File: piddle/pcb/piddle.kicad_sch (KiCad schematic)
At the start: 58 parts, among them J1 Conn_01x03_Socket, J10 Conn_01x03_Socket, J11 Conn_01x03_Socket, J12 Conn_01x03_Socket, J13 Conn_01x03_Socket, J14 Conn_01x03_Socket, J15 Conn_01x03_Socket, J16 infrared receiver, J17 5v, J18 3v3, J19 5v, J2 Conn_01x03_Socket, J20 JST power 1, J21 JST power 2, J22 5V in jumper from LED strip, J23 GPIOs, J24 radio receiver, J25 JST power 3, J3 Conn_01x03_Socket, J4 Conn_01x03_Socket, J5 Conn_01x03_Socket, J6 Conn_01x03_Socket, J7 Conn_01x03_Socket, J8 Conn_01x03_Socket, J9 Conn_01x03_Socket, U1 ESP32-DevKitC, U2 INMP441

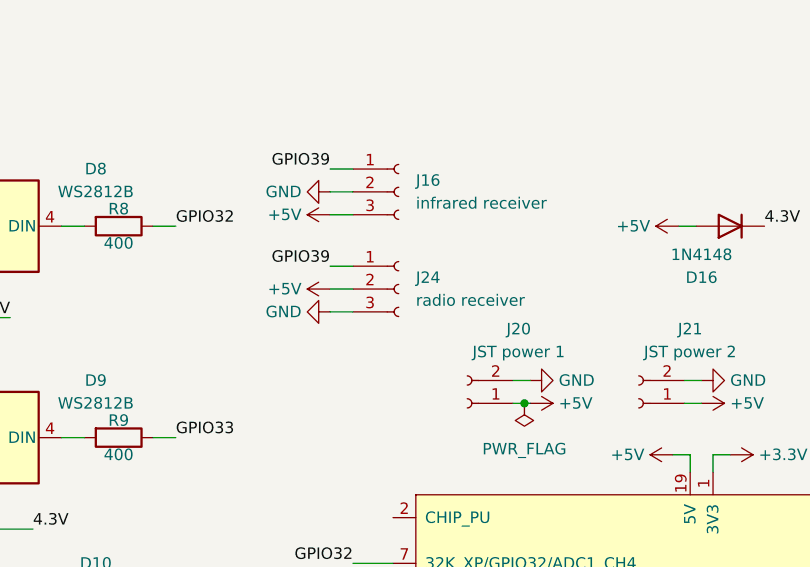
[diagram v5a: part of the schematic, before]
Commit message: Move pins around for RF radio module
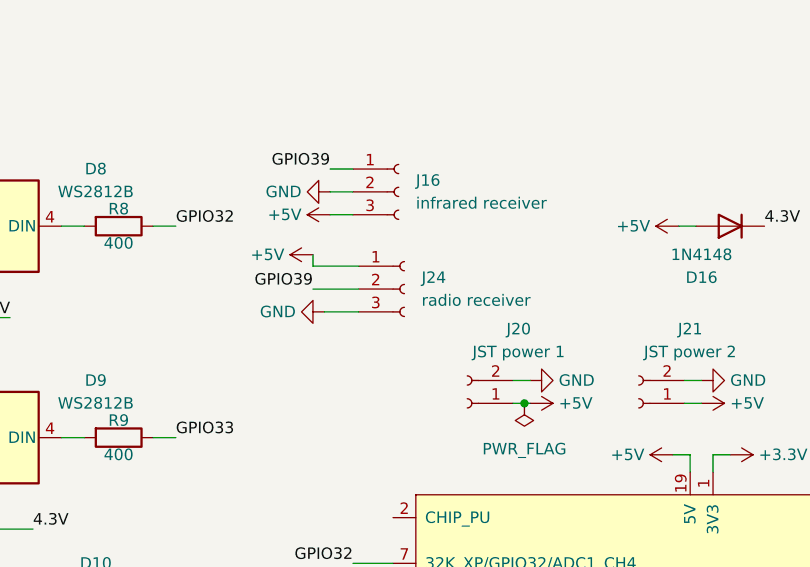
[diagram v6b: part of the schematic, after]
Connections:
- net +5V: now also J24.1 (Pin_1); no longer J24.2 (Pin_2)
- net GPIO39: now also J24.2 (Pin_2); no longer J24.1 (Pin_1)
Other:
- moved on the sheet: J24
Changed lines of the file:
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@@
 	(wire
 		(pts
-			(xy 172.72 115.57) (xy 176.53 115.57)
+			(xy 102.87 26.67) (xy 97.79 26.67)
 		)
 		(stroke
@@
 	(wire
 		(pts
-			(xy 158.75 41.91) (xy 160.655 41.91)
+			(xy 172.72 115.57) (xy 176.53 115.57)
 		)
 		(stroke
@@
 	(wire
 		(pts
-			(xy 99.695 26.67) (xy 102.235 26.67)
+			(xy 158.75 41.91) (xy 160.655 41.91)
 		)
 		(stroke
@@
 	(wire
 		(pts
+			(xy 97.79 26.67) (xy 97.79 25.4)
+		)
+		(stroke
+			(width 0)
+			(type default)
+		)
+	)
+	(wire
+		(pts
 			(xy 223.52 17.78) (xy 224.79 17.78)
 		)
@@
 	(wire
 		(pts
+			(xy 99.06 31.75) (xy 102.87 31.75)
+		)
+		(stroke
+			(width 0)
+			(type default)
+		)
+	)
+	(wire
+		(pts
 			(xy 213.36 55.88) (xy 215.9 55.88)
 		)
@@
 	(wire
 		(pts
-			(xy 137.795 47.625) (xy 139.7 47.625)
+			(xy 97.79 29.21) (xy 102.87 29.21)
 		)
 		(stroke
@@
 	(wire
 		(pts
-			(xy 235.585 103.505) (xy 231.14 103.505)
+			(xy 137.795 47.625) (xy 139.7 47.625)
 		)
 		(stroke
@@
 	(wire
 		(pts
-			(xy 50.165 155.575) (xy 50.165 156.845)
+			(xy 235.585 103.505) (xy 231.14 103.505)
 		)
 		(stroke
@@
 	(wire
 		(pts
-			(xy 223.52 45.72) (xy 223.52 48.26)
+			(xy 50.165 155.575) (xy 50.165 156.845)
 		)
 		(stroke
@@
 	(wire
 		(pts
-			(xy 105.41 169.545) (xy 107.95 169.545)
+			(xy 223.52 45.72) (xy 223.52 48.26)
 		)
 		(stroke
@@
 	(wire
 		(pts
-			(xy 223.52 93.345) (xy 223.52 95.885)
+			(xy 105.41 169.545) (xy 107.95 169.545)
 		)
 		(stroke
@@
 	(wire
 		(pts
-			(xy 72.39 66.04) (xy 69.85 66.04)
+			(xy 223.52 93.345) (xy 223.52 95.885)
 		)
 		(stroke
@@
 	(wire
 		(pts
-			(xy 121.285 41.91) (xy 121.92 41.91)
+			(xy 72.39 66.04) (xy 69.85 66.04)
 		)
 		(stroke
@@
 	(wire
 		(pts
-			(xy 99.695 29.21) (xy 102.235 29.21)
+			(xy 121.285 41.91) (xy 121.92 41.91)
 		)
 		(stroke
@@
 	(wire
 		(pts
-			(xy 99.695 31.75) (xy 102.235 31.75)
-		)
-		(stroke
-			(width 0)
-			(type default)
-		)
-	)
-	(wire
-		(pts
 			(xy 221.615 93.345) (xy 223.52 93.345)
 		)
@@
 	)
 	(label "GPIO39"
-		(at 99.695 26.67 180)
+		(at 97.79 29.21 180)
 		(effects
 			(font
@@
 	(symbol
 		(lib_id "power:+5V")
-		(at 99.695 29.21 90)
+		(at 97.79 25.4 90)
 		(unit 1)
 		(exclude_from_sim no)
@@
 		(on_board yes)
 		(dnp no)
-		(fields_autoplaced yes)
 		(property "Reference" "#PWR032"
-			(at 103.505 29.21 0)
+			(at 101.6 25.4 0)
 			(effects
 				(font
@@
 		)
 		(property "Value" "+5V"
-			(at 96.52 29.21 90)
+			(at 94.615 25.4 90)
 			(effects
 				(font
@@
 		)
 		(property "Footprint" ""
-			(at 99.695 29.21 0)
+			(at 97.79 25.4 0)
 			(effects
 				(font
@@
 		)
 		(property "Datasheet" ""
-			(at 99.695 29.21 0)
+			(at 97.79 25.4 0)
 			(effects
 				(font
@@
 		)
 		(property "Description" ""
-			(at 99.695 29.21 0)
+			(at 97.79 25.4 0)
 			(effects
 				(font
@@
 	(symbol
 		(lib_id "Connector:Conn_01x03_Socket")
-		(at 107.315 29.21 0)
+		(at 107.95 29.21 0)
 		(unit 1)
 		(exclude_from_sim no)
@@
 		(fields_autoplaced yes)
 		(property "Reference" "J24"
-			(at 109.22 27.94 0)
+			(at 109.855 27.94 0)
 			(effects
 				(font
@@
 		)
 		(property "Value" "radio receiver"
-			(at 109.22 30.48 0)
+			(at 109.855 30.48 0)
 			(effects
 				(font
@@
 		)
 		(property "Footprint" "Connector_PinHeader_2.54mm:PinHeader_1x03_P2.54mm_Vertical"
-			(at 107.315 29.21 0)
+			(at 107.95 29.21 0)
 			(effects
 				(font
@@
 		)
 		(property "Datasheet" "~"
-			(at 107.315 29.21 0)
+			(at 107.95 29.21 0)
 			(effects
 				(font
@@
 		)
 		(property "Description" ""
-			(at 107.315 29.21 0)
+			(at 107.95 29.21 0)
 			(effects
 				(font
@@
 	(symbol
 		(lib_id "power:GND")
-		(at 99.695 31.75 270)
+		(at 99.06 31.75 270)
 		(unit 1)
 		(exclude_from_sim no)
@@
 		(dnp no)
 		(property "Reference" "#PWR031"
-			(at 93.345 31.75 0)
+			(at 92.71 31.75 0)
 			(effects
 				(font
@@
 		)
 		(property "Value" "GND"
-			(at 96.52 31.75 90)
+			(at 95.885 31.75 90)
 			(effects
 				(font
@@
 		)
 		(property "Footprint" ""
-			(at 99.695 31.75 0)
+			(at 99.06 31.75 0)
 			(effects
 				(font
@@
 		)
 		(property "Datasheet" ""
-			(at 99.695 31.75 0)
+			(at 99.06 31.75 0)
 			(effects
 				(font
@@
 		)
 		(property "Description" ""
-			(at 99.695 31.75 0)
+			(at 99.06 31.75 0)
 			(effects
 				(font

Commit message: Don't use pins used by WiFi
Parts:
- D1, D10, D11, D12, D13, D14, D15, D2, D3, D4, D5, D6, D7, D8, D9: footprint LED_SMD:LED_WS2812B_PLCC4_5.0x5.0mm_P3.2mm -> PCM_JLCPCB:LED_WS2812B_PLCC4_5.0x5.0mm_P3.2mm
- R1, R10, R11, R12, R13, R14, R15, R2, R3, R4, R5, R6, R7, R8, R9: footprint Resistor_THT:R_Axial_DIN0207_L6.3mm_D2.5mm_P10.16mm_Horizontal -> PCM_JLCPCB:R_1206
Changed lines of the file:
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@@
 			)
 		)
-		(property "Footprint" "LED_SMD:LED_WS2812B_PLCC4_5.0x5.0mm_P3.2mm"
+		(property "Footprint" "PCM_JLCPCB:LED_WS2812B_PLCC4_5.0x5.0mm_P3.2mm"
 			(at 224.79 159.385 0)
 			(effects
@@
 			)
 		)
-		(property "Footprint" "Resistor_THT:R_Axial_DIN0207_L6.3mm_D2.5mm_P10.16mm_Horizontal"
+		(property "Footprint" "PCM_JLCPCB:R_1206"
 			(at 209.55 130.683 90)
 			(effects
@@
 			)
 		)
-		(property "Footprint" "Resistor_THT:R_Axial_DIN0207_L6.3mm_D2.5mm_P10.16mm_Horizontal"
+		(property "Footprint" "PCM_JLCPCB:R_1206"
 			(at 209.55 77.597 90)
 			(effects
@@
 			)
 		)
-		(property "Footprint" "Resistor_THT:R_Axial_DIN0207_L6.3mm_D2.5mm_P10.16mm_Horizontal"
+		(property "Footprint" "PCM_JLCPCB:R_1206"
 			(at 76.2 64.262 90)
 			(effects
@@
 			)
 		)
-		(property "Footprint" "Resistor_THT:R_Axial_DIN0207_L6.3mm_D2.5mm_P10.16mm_Horizontal"
+		(property "Footprint" "PCM_JLCPCB:R_1206"
 			(at 209.55 57.658 90)
 			(effects
@@
 			)
 		)
-		(property "Footprint" "Resistor_THT:R_Axial_DIN0207_L6.3mm_D2.5mm_P10.16mm_Horizontal"
+		(property "Footprint" "PCM_JLCPCB:R_1206"
 			(at 76.2 182.372 90)
 			(effects
@@
 			)
 		)
-		(property "Footprint" "Resistor_THT:R_Axial_DIN0207_L6.3mm_D2.5mm_P10.16mm_Horizontal"
+		(property "Footprint" "PCM_JLCPCB:R_1206"
 			(at 76.2 129.667 90)
 			(effects
@@
 			)
 		)
-		(property "Footprint" "LED_SMD:LED_WS2812B_PLCC4_5.0x5.0mm_P3.2mm"
+		(property "Footprint" "PCM_JLCPCB:LED_WS2812B_PLCC4_5.0x5.0mm_P3.2mm"
 			(at 60.96 123.825 0)
 			(effects
@@
 			)
 		)
-		(property "Footprint" "LED_SMD:LED_WS2812B_PLCC4_5.0x5.0mm_P3.2mm"
+		(property "Footprint" "PCM_JLCPCB:LED_WS2812B_PLCC4_5.0x5.0mm_P3.2mm"
 			(at 224.79 136.525 0)
 			(effects
@@
 			)
 		)
-		(property "Footprint" "LED_SMD:LED_WS2812B_PLCC4_5.0x5.0mm_P3.2mm"
+		(property "Footprint" "PCM_JLCPCB:LED_WS2812B_PLCC4_5.0x5.0mm_P3.2mm"
 			(at 60.96 101.6 0)
 			(effects
@@
 			)
 		)
-		(property "Footprint" "LED_SMD:LED_WS2812B_PLCC4_5.0x5.0mm_P3.2mm"
+		(property "Footprint" "PCM_JLCPCB:LED_WS2812B_PLCC4_5.0x5.0mm_P3.2mm"
 			(at 224.79 111.125 0)
 			(effects
@@
 			)
 		)
-		(property "Footprint" "Resistor_THT:R_Axial_DIN0207_L6.3mm_D2.5mm_P10.16mm_Horizontal"
+		(property "Footprint" "PCM_JLCPCB:R_1206"
 			(at 209.55 11.938 90)
 			(effects
@@
 			)
 		)
-		(property "Footprint" "Resistor_THT:R_Axial_DIN0207_L6.3mm_D2.5mm_P10.16mm_Horizontal"
+		(property "Footprint" "PCM_JLCPCB:R_1206"
 			(at 209.55 35.433 90)
 			(effects
@@
 			)
 		)
-		(property "Footprint" "LED_SMD:LED_WS2812B_PLCC4_5.0x5.0mm_P3.2mm"
+		(property "Footprint" "PCM_JLCPCB:LED_WS2812B_PLCC4_5.0x5.0mm_P3.2mm"
 			(at 60.96 38.1 0)
 			(effects
@@
 			)
 		)
-		(property "Footprint" "Resistor_THT:R_Axial_DIN0207_L6.3mm_D2.5mm_P10.16mm_Horizontal"
+		(property "Footprint" "PCM_JLCPCB:R_1206"
 			(at 209.55 153.543 90)
 			(effects
@@
 			)
 		)
-		(property "Footprint" "Resistor_THT:R_Axial_DIN0207_L6.3mm_D2.5mm_P10.16mm_Horizontal"
+		(property "Footprint" "PCM_JLCPCB:R_1206"
 			(at 209.55 105.283 90)
 			(effects
@@
 			)
 		)
-		(property "Footprint" "LED_SMD:LED_WS2812B_PLCC4_5.0x5.0mm_P3.2mm"
+		(property "Footprint" "PCM_JLCPCB:LED_WS2812B_PLCC4_5.0x5.0mm_P3.2mm"
 			(at 60.96 80.01 0)
 			(effects
@@
 			)
 		)
-		(property "Footprint" "LED_SMD:LED_WS2812B_PLCC4_5.0x5.0mm_P3.2mm"
+		(property "Footprint" "PCM_JLCPCB:LED_WS2812B_PLCC4_5.0x5.0mm_P3.2mm"
 			(at 224.79 86.995 0)
 			(effects
@@
 			)
 		)
-		(property "Footprint" "LED_SMD:LED_WS2812B_PLCC4_5.0x5.0mm_P3.2mm"
+		(property "Footprint" "PCM_JLCPCB:LED_WS2812B_PLCC4_5.0x5.0mm_P3.2mm"
 			(at 60.96 58.42 0)
 			(effects
@@
 			)
 		)
-		(property "Footprint" "LED_SMD:LED_WS2812B_PLCC4_5.0x5.0mm_P3.2mm"
+		(property "Footprint" "PCM_JLCPCB:LED_WS2812B_PLCC4_5.0x5.0mm_P3.2mm"
 			(at 60.96 14.605 0)
 			(effects
@@
 			)
 		)
-		(property "Footprint" "Resistor_THT:R_Axial_DIN0207_L6.3mm_D2.5mm_P10.16mm_Horizontal"
+		(property "Footprint" "PCM_JLCPCB:R_1206"
 			(at 76.2 43.942 90)
 			(effects
@@
 			)
 		)
-		(property "Footprint" "Resistor_THT:R_Axial_DIN0207_L6.3mm_D2.5mm_P10.16mm_Horizontal"
+		(property "Footprint" "PCM_JLCPCB:R_1206"
 			(at 76.2 85.852 90)
 			(effects
@@
 			)
 		)
-		(property "Footprint" "LED_SMD:LED_WS2812B_PLCC4_5.0x5.0mm_P3.2mm"
+		(property "Footprint" "PCM_JLCPCB:LED_WS2812B_PLCC4_5.0x5.0mm_P3.2mm"
 			(at 60.96 176.53 0)
 			(effects
@@
 			)
 		)
-		(property "Footprint" "LED_SMD:LED_WS2812B_PLCC4_5.0x5.0mm_P3.2mm"
+		(property "Footprint" "PCM_JLCPCB:LED_WS2812B_PLCC4_5.0x5.0mm_P3.2mm"
 			(at 224.79 17.78 0)
 			(effects
@@
 			)
 		)
-		(property "Footprint" "LED_SMD:LED_WS2812B_PLCC4_5.0x5.0mm_P3.2mm"
+		(property "Footprint" "PCM_JLCPCB:LED_WS2812B_PLCC4_5.0x5.0mm_P3.2mm"
 			(at 224.79 63.5 0)
 			(effects
@@
 			)
 		)
-		(property "Footprint" "LED_SMD:LED_WS2812B_PLCC4_5.0x5.0mm_P3.2mm"
+		(property "Footprint" "PCM_JLCPCB:LED_WS2812B_PLCC4_5.0x5.0mm_P3.2mm"
 			(at 60.96 145.415 0)
 			(effects
@@
 			)
 		)
-		(property "Footprint" "Resistor_THT:R_Axial_DIN0207_L6.3mm_D2.5mm_P10.16mm_Horizontal"
+		(property "Footprint" "PCM_JLCPCB:R_1206"
 			(at 76.2 20.447 90)
 			(effects
@@
 			)
 		)
-		(property "Footprint" "LED_SMD:LED_WS2812B_PLCC4_5.0x5.0mm_P3.2mm"
+		(property "Footprint" "PCM_JLCPCB:LED_WS2812B_PLCC4_5.0x5.0mm_P3.2mm"
 			(at 224.79 41.275 0)
 			(effects
@@
 			)
 		)
-		(property "Footprint" "Resistor_THT:R_Axial_DIN0207_L6.3mm_D2.5mm_P10.16mm_Horizontal"
+		(property "Footprint" "PCM_JLCPCB:R_1206"
 			(at 76.2 107.442 90)
 			(effects
@@
 			)
 		)
-		(property "Footprint" "Resistor_THT:R_Axial_DIN0207_L6.3mm_D2.5mm_P10.16mm_Horizontal"
+		(property "Footprint" "PCM_JLCPCB:R_1206"
 			(at 76.2 151.257 90)
 			(effects

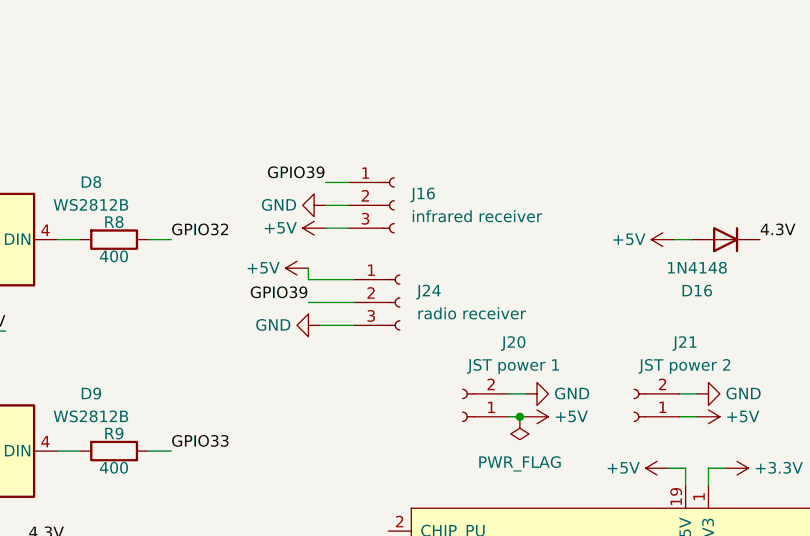
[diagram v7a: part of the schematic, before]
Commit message: Add 433 MHz radio receiver pins
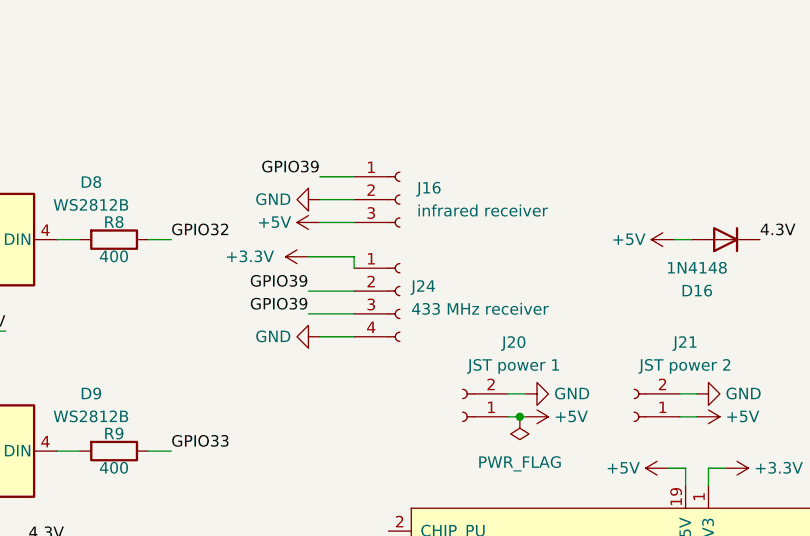
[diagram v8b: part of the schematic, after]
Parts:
- removed J24: radio receiver, Connector_PinHeader_2.54mm:PinHeader_1x03_P2.54mm_Vertical, symbol Connector:Conn_01x03_Socket
- added J24: 433 MHz receiver, Connector_PinHeader_2.54mm:PinHeader_1x04_P2.54mm_Vertical, symbol Connector:Conn_01x04_Socket
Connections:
- net +3.3V: now also J24.1 (Pin_1)
- net GND: now also J24.4 (Pin_4)
- net GPIO39: now also J24.2 (Pin_2), J24.3 (Pin_3)
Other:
- moved on the sheet: J16
